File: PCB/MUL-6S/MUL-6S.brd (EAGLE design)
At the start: 35.5 x 18.8 mm, 22 parts

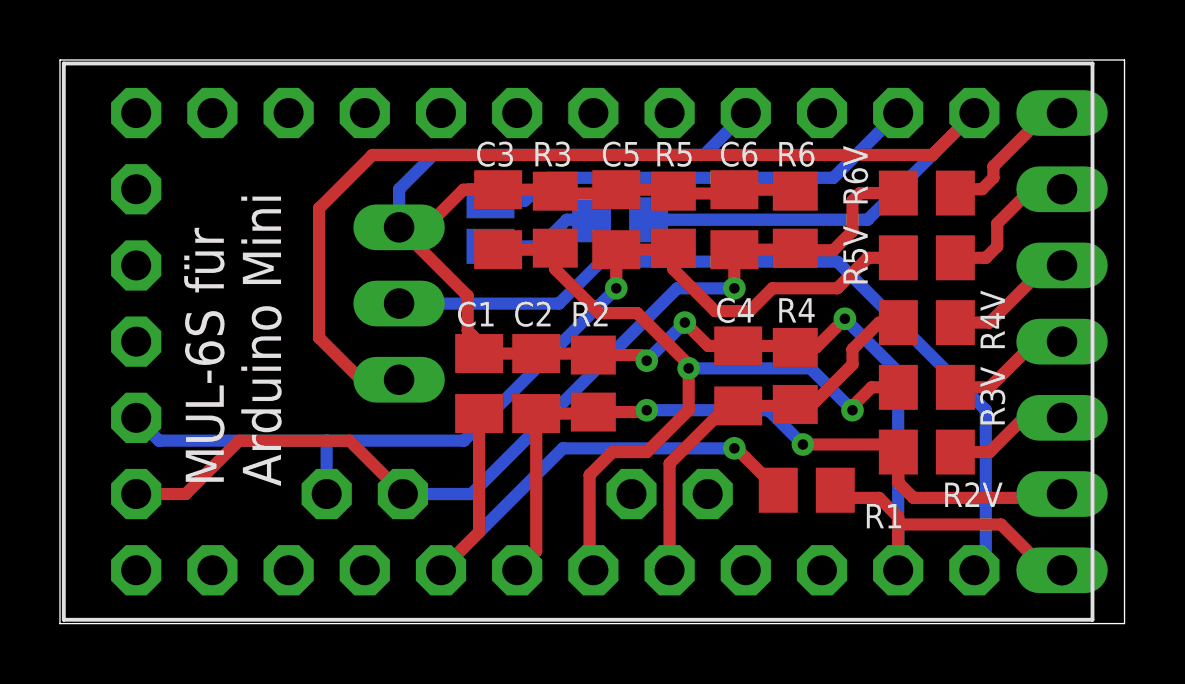
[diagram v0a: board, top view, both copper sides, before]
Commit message: Zelle 1 war falsch angeschlossen
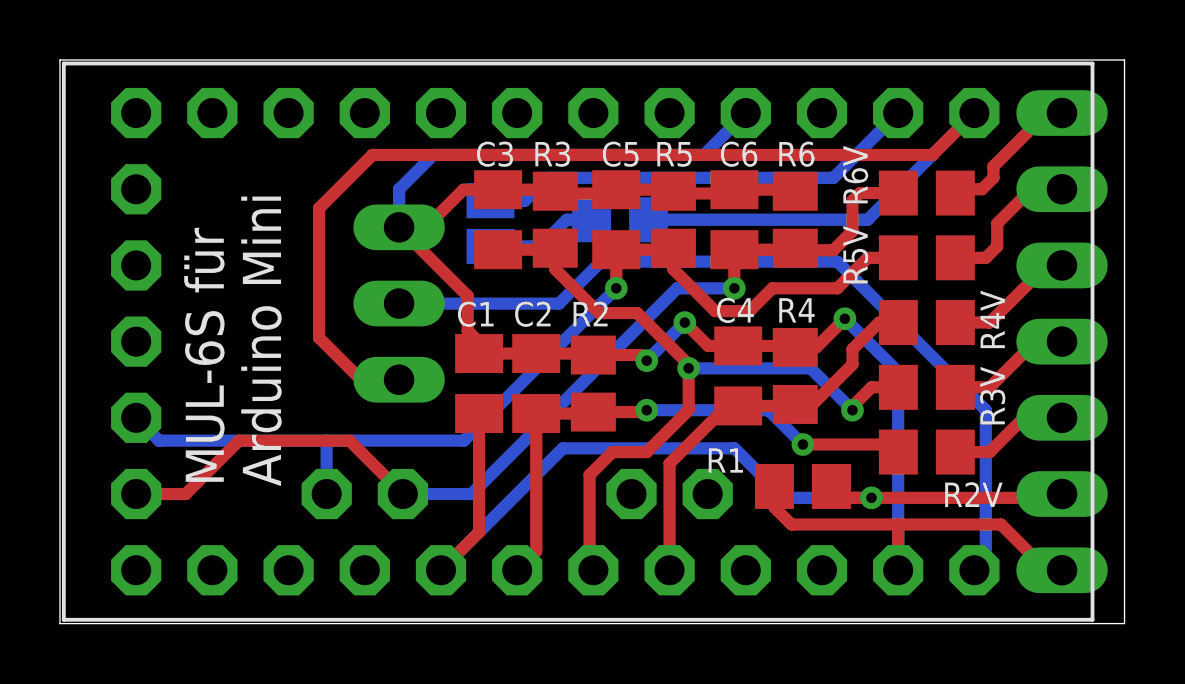
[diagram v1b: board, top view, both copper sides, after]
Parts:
- moved R1 0.18 mm to (54.0, 32.0), turned to 180 degrees
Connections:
- net N$10: now also AKKU.2
- net N$19: no longer AKKU.2
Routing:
- net N$10: track 19.3 -> 30.4 mm
- net N$19: track 24.9 -> 18.2 mm
- net GND: track 66.2 -> 68.5 mm
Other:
- board text added: "MUL-6S V1.02 (c) 06.03.2020 Th. Lehmann thomas@thls.de"
- board text removed: "MUL-6S V1.01 (c) 18.01.2020 Th. Lehmann thomas@thls.de"
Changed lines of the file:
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@@
 <drawing>
 <settings>
-<setting alwaysvectorfont="yes"/>
+<setting alwaysvectorfont="no"/>
 <setting verticaltext="up"/>
 </settings>
@@
 <layer number="23" name="tOrigins" color="15" fill="1" visible="yes" active="yes"/>
 <layer number="24" name="bOrigins" color="15" fill="1" visible="yes" active="yes"/>
-<layer number="25" name="tNames" color="7" fill="1" visible="no" active="yes"/>
+<layer number="25" name="tNames" color="7" fill="1" visible="yes" active="yes"/>
 <layer number="26" name="bNames" color="7" fill="1" visible="yes" active="yes"/>
 <layer number="27" name="tValues" color="7" fill="1" visible="no" active="yes"/>
@@
 <text x="53.594" y="32.385" size="1.016" layer="26" rot="MR0">Z1</text>
 <text x="54.229" y="30.226" size="0.8128" layer="26" rot="MR0">GND</text>
-<text x="42.545" y="30.226" size="0.8128" layer="26" rot="MR90">MUL-6S V1.01
-(c) 18.01.2020
+<text x="42.545" y="30.226" size="0.8128" layer="26" rot="MR90">MUL-6S V1.02
+(c) 06.03.2020
 Th. Lehmann
 thomas@thls.de</text>
@@
 <attribute name="VALUE" x="39.878" y="34.29" size="1.27" layer="27" rot="SR90"/>
 </element>
-<element name="R1" library="resistor" library_urn="urn:adsk.eagle:library:348" package="R0805" package3d_urn="urn:adsk.eagle:package:23553/2" value="1K" x="54.102" y="31.877" smashed="yes">
-<attribute name="NAME" x="56.007" y="30.607" size="0.8128" layer="25" ratio="10"/>
-<attribute name="VALUE" x="50.5714" y="31.242" size="1.27" layer="27" ratio="10" display="off"/>
+<element name="R1" library="resistor" library_urn="urn:adsk.eagle:library:348" package="R0805" package3d_urn="urn:adsk.eagle:package:23553/2" value="1K" x="53.975" y="32.004" smashed="yes" rot="R180">
+<attribute name="NAME" x="52.07" y="33.274" size="0.8128" layer="25" ratio="10" rot="R180"/>
+<attribute name="VALUE" x="57.5056" y="32.639" size="1.27" layer="27" ratio="10" rot="R180" display="off"/>
 </element>
 <element name="R2" library="resistor" library_urn="urn:adsk.eagle:library:348" package="R0805" package3d_urn="urn:adsk.eagle:package:23553/2" value="1K" x="46.99" y="35.433" smashed="yes" rot="R90">
@@
 <contactref element="AKKU" pad="1"/>
 <wire x1="57.15" y1="35.814" x2="57.15" y2="29.21" width="0.4064" layer="16"/>
-<wire x1="55.306" y1="31.623" x2="55.052" y2="31.877" width="0.4064" layer="1"/>
-<wire x1="56.515" y1="31.623" x2="55.306" y2="31.623" width="0.4064" layer="1"/>
 <wire x1="55.372" y1="37.592" x2="54.417" y2="36.637" width="0.4064" layer="1"/>
 <wire x1="54.417" y1="36.637" x2="53.721" y2="36.637" width="0.4064" layer="1"/>
 <wire x1="43.815" y1="41.894" x2="45.67" y2="41.894" width="0.4064" layer="1"/>
 <wire x1="45.67" y1="41.894" x2="45.72" y2="41.844" width="0.4064" layer="1"/>
-<wire x1="56.515" y1="31.623" x2="57.15" y2="30.988" width="0.4064" layer="1"/>
-<wire x1="57.15" y1="30.988" x2="57.15" y2="30.734" width="0.4064" layer="1"/>
 <wire x1="57.15" y1="30.734" x2="57.15" y2="29.21" width="0.4064" layer="1"/>
 <wire x1="42.799" y1="38.354" x2="42.799" y2="37.195" width="0.4064" layer="1"/>
@@
 <wire x1="45.72" y1="41.844" x2="45.797" y2="41.767" width="0.4064" layer="1"/>
 <wire x1="47.625" y1="41.767" x2="45.797" y2="41.767" width="0.4064" layer="1"/>
+<wire x1="53.025" y1="31.303" x2="53.025" y2="32.004" width="0.4064" layer="1"/>
+<wire x1="57.15" y1="30.734" x2="53.594" y2="30.734" width="0.4064" layer="1"/>
+<wire x1="53.594" y1="30.734" x2="53.025" y2="31.303" width="0.4064" layer="1"/>
 </signal>
 <signal name="N$10">
@@
 <wire x1="43.18" y1="34.433" x2="43.18" y2="30.48" width="0.4064" layer="1"/>
 <wire x1="43.18" y1="30.48" x2="41.91" y2="29.21" width="0.4064" layer="1"/>
-<wire x1="51.689" y1="33.274" x2="45.974" y2="33.274" width="0.4064" layer="16"/>
+<wire x1="45.974" y1="33.274" x2="51.689" y2="33.274" width="0.4064" layer="16"/>
 <wire x1="45.974" y1="33.274" x2="41.91" y2="29.21" width="0.4064" layer="16"/>
-<wire x1="53.152" y1="31.877" x2="52.0395" y2="32.9895" width="0.4064" layer="1"/>
-<wire x1="52.0395" y1="32.9895" x2="51.755" y2="33.274" width="0.4064" layer="1"/>
-<wire x1="51.755" y1="33.274" x2="51.689" y2="33.274" width="0.4064" layer="1"/>
-<via x="51.689" y="33.274" extent="1-16" drill="0.35"/>
+<contactref element="AKKU" pad="2"/>
+<wire x1="54.925" y1="32.004" x2="54.991" y2="32.004" width="0.4064" layer="1"/>
+<wire x1="54.991" y1="32.004" x2="55.372" y2="31.623" width="0.4064" layer="1"/>
+<wire x1="55.372" y1="31.623" x2="56.261" y2="31.623" width="0.4064" layer="1"/>
+<wire x1="56.261" y1="31.623" x2="62.484" y2="31.623" width="0.4064" layer="1"/>
+<wire x1="62.484" y1="31.623" x2="62.611" y2="31.75" width="0.4064" layer="1"/>
+<wire x1="51.689" y1="33.274" x2="53.34" y2="31.623" width="0.4064" layer="16"/>
+<wire x1="53.34" y1="31.623" x2="56.261" y2="31.623" width="0.4064" layer="16"/>
+<via x="56.261" y="31.623" extent="1-16" drill="0.35"/>
 </signal>
 <signal name="N$19">
@@
 <wire x1="45.085" y1="34.433" x2="46.94" y2="34.433" width="0.4064" layer="1"/>
 <wire x1="46.94" y1="34.433" x2="46.99" y2="34.483" width="0.4064" layer="1"/>
-<contactref element="AKKU" pad="2"/>
-<wire x1="57.155" y1="32.126" x2="57.155" y2="33.147" width="0.4064" layer="1"/>
-<wire x1="62.611" y1="31.75" x2="62.484" y2="31.623" width="0.4064" layer="1"/>
-<wire x1="62.484" y1="31.623" x2="57.658" y2="31.623" width="0.4064" layer="1"/>
-<wire x1="57.658" y1="31.623" x2="57.155" y2="32.126" width="0.4064" layer="1"/>
 <wire x1="53.975" y1="33.401" x2="56.901" y2="33.401" width="0.4064" layer="1"/>
 <wire x1="56.901" y1="33.401" x2="57.155" y2="33.147" width="0.4064" layer="1"/>
@@
 <contactref element="U$1" pad="A7-I"/>
 <contactref element="R6V" pad="1"/>
-<wire x1="57.155" y1="41.783" x2="56.896" y2="41.783" width="0.4064" layer="1"/>
 <wire x1="40.64" y1="31.75" x2="42.926" y2="31.75" width="0.4064" layer="16"/>
 <wire x1="49.784" y1="38.608" x2="42.926" y2="31.75" width="0.4064" layer="16"/>
@@
 <wire x1="53.671" y1="39.894" x2="53.721" y2="39.944" width="0.4064" layer="1"/>
 <wire x1="51.689" y1="38.608" x2="51.689" y2="39.894" width="0.4064" layer="1"/>
-<wire x1="57.155" y1="41.783" x2="55.88" y2="41.783" width="0.4064" layer="1"/>
 <wire x1="55.626" y1="41.529" x2="55.626" y2="40.513" width="0.4064" layer="1"/>
 <wire x1="55.626" y1="40.513" x2="54.991" y2="39.878" width="0.4064" layer="1"/>
-<wire x1="55.88" y1="41.783" x2="55.626" y2="41.529" width="0.4064" layer="1"/>
+<wire x1="55.626" y1="41.529" x2="55.88" y2="41.783" width="0.4064" layer="1"/>
+<wire x1="55.88" y1="41.783" x2="57.155" y2="41.783" width="0.4064" layer="1"/>
 </signal>
 <signal name="N$4">
